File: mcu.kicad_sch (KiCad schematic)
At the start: 14 parts, among them U4 STM32F070RBTx, Y2 XRCGB32M000F2P01R0

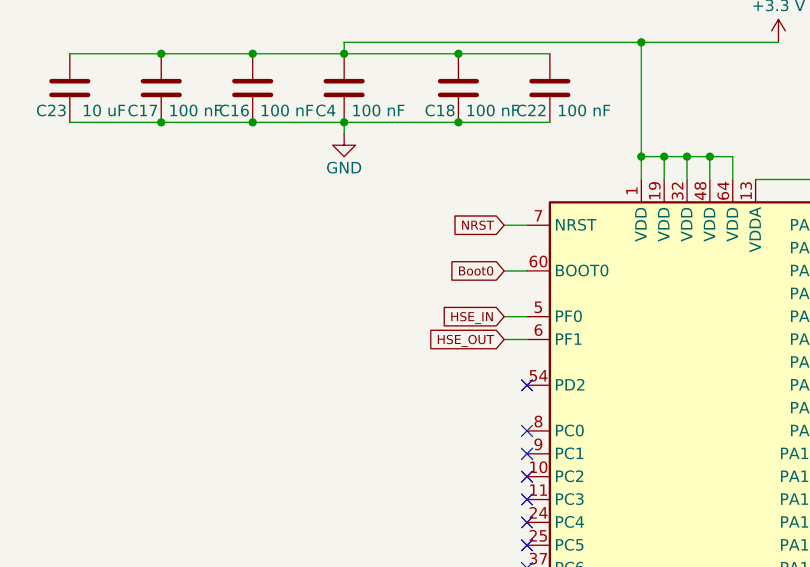
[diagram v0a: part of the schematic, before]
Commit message: removed manual switch
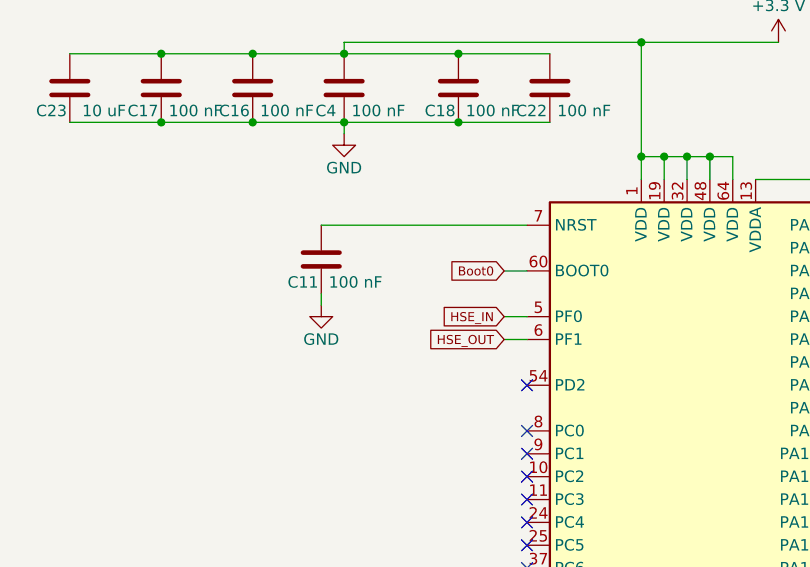
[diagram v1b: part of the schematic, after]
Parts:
- added C11: 100 nF, Capacitor_SMD:C_0805_2012Metric, symbol Device:C
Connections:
- net GND: now also C11.1
- net NRST: no longer names the net of U4.7 (NRST)
- net NRST: now also C11.2
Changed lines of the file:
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@@
+	(wire
+		(pts
+			(xy 63.5 66.04) (xy 63.5 67.31)
+		)
+		(stroke
+			(width 0)
+			(type default)
+		)
+	)
 	(wire
 		(pts
@@
 	(wire
 		(pts
+			(xy 63.5 58.42) (xy 86.36 58.42)
+		)
+		(stroke
+			(width 0)
+			(type default)
+		)
+	)
+	(wire
+		(pts
 			(xy 204.47 91.44) (xy 204.47 86.36)
 		)
@@
 		(pts
 			(xy 101.6 53.34) (xy 101.6 50.8)
-		)
-		(stroke
-			(width 0)
-			(type default)
-		)
-	)
-	(wire
-		(pts
-			(xy 83.82 58.42) (xy 86.36 58.42)
 		)
 		(stroke
@@
 		)
 	)
-	(global_label "NRST"
-		(shape input)
-		(at 83.82 58.42 180)
-		(fields_autoplaced yes)
-		(effects
-			(font
-				(size 1 1)
-			)
-			(justify right)
-		)
-		(property "Intersheetrefs" "${INTERSHEET_REFS}"
-			(at 77.7078 58.42 0)
-			(effects
-				(font
-					(size 1.27 1.27)
-				)
-				(justify right)
-				(hide yes)
-			)
-		)
-	)
 	(global_label "USART1_RX"
 		(shape input)
@@
 	(symbol
 		(lib_id "power:GND")
+		(at 63.5 67.31 0)
+		(unit 1)
+		(exclude_from_sim no)
+		(in_bom yes)
+		(on_board yes)
+		(dnp no)
+		(property "Reference" "#PWR021"
+			(at 63.5 73.66 0)
+			(effects
+				(font
+					(size 1.27 1.27)
+				)
+				(hide yes)
+			)
+		)
+		(property "Value" "GND"
+			(at 63.5 71.12 0)
+			(effects
+				(font
+					(size 1.27 1.27)
+				)
+			)
+		)
+		(property "Footprint" ""
+			(at 63.5 67.31 0)
+			(effects
+				(font
+					(size 1.27 1.27)
+				)
+				(hide yes)
+			)
+		)
+		(property "Datasheet" ""
+			(at 63.5 67.31 0)
+			(effects
+				(font
+					(size 1.27 1.27)
+				)
+				(hide yes)
+			)
+		)
+		(property "Description" "Power symbol creates a global label with name \"GND\" , ground"
+			(at 63.5 67.31 0)
+			(effects
+				(font
+					(size 1.27 1.27)
+				)
+				(hide yes)
+			)
+		)
+		(pin "1"
+		)
+		(instances
+			(project "apex"
+				(path "/84b8b555-aaa5-476b-b0f2-2d0f894bf0e6/365404b6-d1fa-4571-8ebc-5e079dd57407"
+					(reference "#PWR021")
+					(unit 1)
+				)
+			)
+		)
+	)
+	(symbol
+		(lib_id "power:GND")
 		(at 137.16 63.5 0)
 		(unit 1)
@@
 					(unit 1)
 				)
+			)
+		)
+	)
+	(symbol
+		(lib_id "Device:C")
+		(at 63.5 62.23 180)
+		(unit 1)
+		(exclude_from_sim no)
+		(in_bom yes)
+		(on_board yes)
+		(dnp no)
+		(property "Reference" "C11"
+			(at 61.468 64.77 0)
+			(effects
+				(font
+					(size 1.27 1.27)
+				)
+			)
+		)
+		(property "Value" "100 nF"
+			(at 67.31 64.77 0)
+			(effects
+				(font
+					(size 1.27 1.27)
+				)
+			)
+		)
+		(property "Footprint" "Capacitor_SMD:C_0805_2012Metric"
+			(at 62.5348 58.42 0)
+			(effects
+				(font
+					(size 1.27 1.27)
+				)
+				(hide yes)
+			)
+		)
+		(property "Datasheet" "~"
+			(at 63.5 62.23 0)
+			(effects
+				(font
+					(size 1.27 1.27)
+				)
+				(hide yes)
+			)
+		)
+		(property "Description" "Unpolarized capacitor"
+			(at 63.5 62.23 0)
+			(effects
+				(font
+					(size 1.27 1.27)
+				)
+				(hide yes)
+			)
+		)
+		(pin "1"
+		)
+		(pin "2"
+		)
+		(instances
+			(project "apex"
+				(path "/84b8b555-aaa5-476b-b0f2-2d0f894bf0e6/365404b6-d1fa-4571-8ebc-5e079dd57407"
+					(reference "C11")
+					(unit 1)
+				)

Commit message: removed AVR mcu
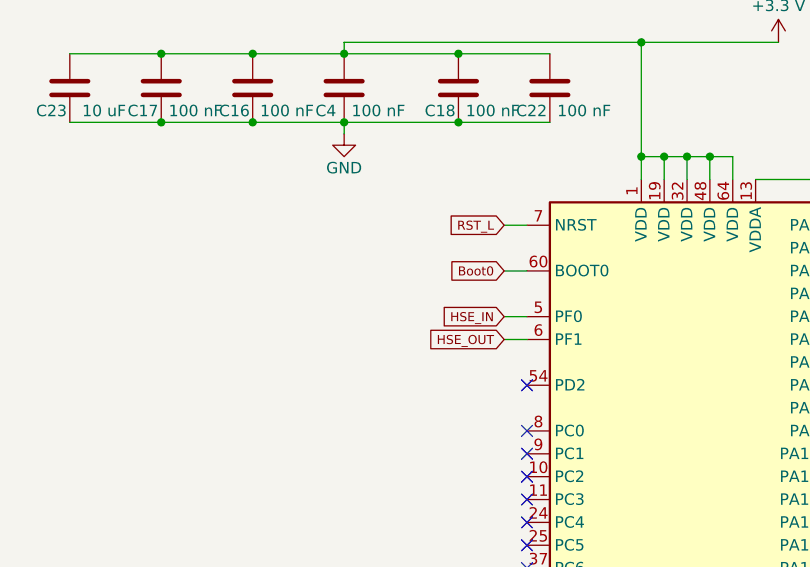
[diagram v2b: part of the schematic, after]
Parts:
- removed C11: 100 nF, Capacitor_SMD:C_0805_2012Metric, symbol Device:C
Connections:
- net RST_L: now reaches U4.7 (NRST)
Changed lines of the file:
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@@
-	(wire
-		(pts
-			(xy 63.5 66.04) (xy 63.5 67.31)
-		)
-		(stroke
-			(width 0)
-			(type default)
-		)
-	)
 	(wire
 		(pts
@@
 	(wire
 		(pts
-			(xy 63.5 58.42) (xy 86.36 58.42)
-		)
-		(stroke
-			(width 0)
-			(type default)
-		)
-	)
-	(wire
-		(pts
 			(xy 204.47 91.44) (xy 204.47 86.36)
 		)
@@
 		(pts
 			(xy 121.92 83.82) (xy 124.46 83.82)
+		)
+		(stroke
+			(width 0)
+			(type default)
+		)
+	)
+	(wire
+		(pts
+			(xy 83.82 58.42) (xy 86.36 58.42)
 		)
 		(stroke
@@
 				)
 				(justify left)
+				(hide yes)
+			)
+		)
+	)
+	(global_label "RST_L"
+		(shape input)
+		(at 83.82 58.42 180)
+		(fields_autoplaced yes)
+		(effects
+			(font
+				(size 1 1)
+			)
+			(justify right)
+		)
+		(property "Intersheetrefs" "${INTERSHEET_REFS}"
+			(at 77.184 58.42 0)
+			(effects
+				(font
+					(size 1.27 1.27)
+				)
+				(justify right)
 				(hide yes)
 			)
@@
 				(path "/84b8b555-aaa5-476b-b0f2-2d0f894bf0e6/365404b6-d1fa-4571-8ebc-5e079dd57407"
 					(reference "#PWR038")
-					(unit 1)
-				)
-			)
-		)
-	)
-	(symbol
-		(lib_id "power:GND")
-		(at 63.5 67.31 0)
-		(unit 1)
-		(exclude_from_sim no)
-		(in_bom yes)
-		(on_board yes)
-		(dnp no)
-		(property "Reference" "#PWR021"
-			(at 63.5 73.66 0)
-			(effects
-				(font
-					(size 1.27 1.27)
-				)
-				(hide yes)
-			)
-		)
-		(property "Value" "GND"
-			(at 63.5 71.12 0)
-			(effects
-				(font
-					(size 1.27 1.27)
-				)
-			)
-		)
-		(property "Footprint" ""
-			(at 63.5 67.31 0)
-			(effects
-				(font
-					(size 1.27 1.27)
-				)
-				(hide yes)
-			)
-		)
-		(property "Datasheet" ""
-			(at 63.5 67.31 0)
-			(effects
-				(font
-					(size 1.27 1.27)
-				)
-				(hide yes)
-			)
-		)
-		(property "Description" "Power symbol creates a global label with name \"GND\" , ground"
-			(at 63.5 67.31 0)
-			(effects
-				(font
-					(size 1.27 1.27)
-				)
-				(hide yes)
-			)
-		)
-		(pin "1"
-		)
-		(instances
-			(project "apex"
-				(path "/84b8b555-aaa5-476b-b0f2-2d0f894bf0e6/365404b6-d1fa-4571-8ebc-5e079dd57407"
-					(reference "#PWR021")
 					(unit 1)
 				)
@@
 					(unit 1)
 				)
-			)
-		)
-	)
-	(symbol
-		(lib_id "Device:C")
-		(at 63.5 62.23 180)
-		(unit 1)
-		(exclude_from_sim no)
-		(in_bom yes)
-		(on_board yes)
-		(dnp no)
-		(property "Reference" "C11"
-			(at 61.468 64.77 0)
-			(effects
-				(font
-					(size 1.27 1.27)
-				)
-			)
-		)
-		(property "Value" "100 nF"
-			(at 67.31 64.77 0)
-			(effects
-				(font
-					(size 1.27 1.27)
-				)
-			)
-		)
-		(property "Footprint" "Capacitor_SMD:C_0805_2012Metric"
-			(at 62.5348 58.42 0)
-			(effects
-				(font
-					(size 1.27 1.27)
-				)
-				(hide yes)
-			)
-		)
-		(property "Datasheet" "~"
-			(at 63.5 62.23 0)
-			(effects
-				(font
-					(size 1.27 1.27)
-				)
-				(hide yes)
-			)
-		)
-		(property "Description" "Unpolarized capacitor"
-			(at 63.5 62.23 0)
-			(effects
-				(font
-					(size 1.27 1.27)
-				)
-				(hide yes)
-			)
-		)
-		(pin "1"
-		)
-		(pin "2"
-		)
-		(instances
-			(project "apex"
-				(path "/84b8b555-aaa5-476b-b0f2-2d0f894bf0e6/365404b6-d1fa-4571-8ebc-5e079dd57407"
-					(reference "C11")
-					(unit 1)
-				)

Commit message: added diode
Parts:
- removed C5, C6: 8 pF, Capacitor_SMD:C_0805_2012Metric, symbol Device:C
- removed Y2: XRCGB32M000F2P01R0, XRCGB32M000F2P01R0:OSC_XRCGB32M000F2P01R0, symbol XRCGB32M000F2P01R0:XRCGB32M000F2P01R0
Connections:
- net +3.3 V renamed VMCU
- net +3.3 VA renamed +3.3VA
- net HSE_IN renamed CLK_32MHZ
- net HSE_OUT: no longer names the net of U4.6 (PF1)
- no-connect marks 41 -> 42
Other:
- note removed: "High-Speed Oscillator"

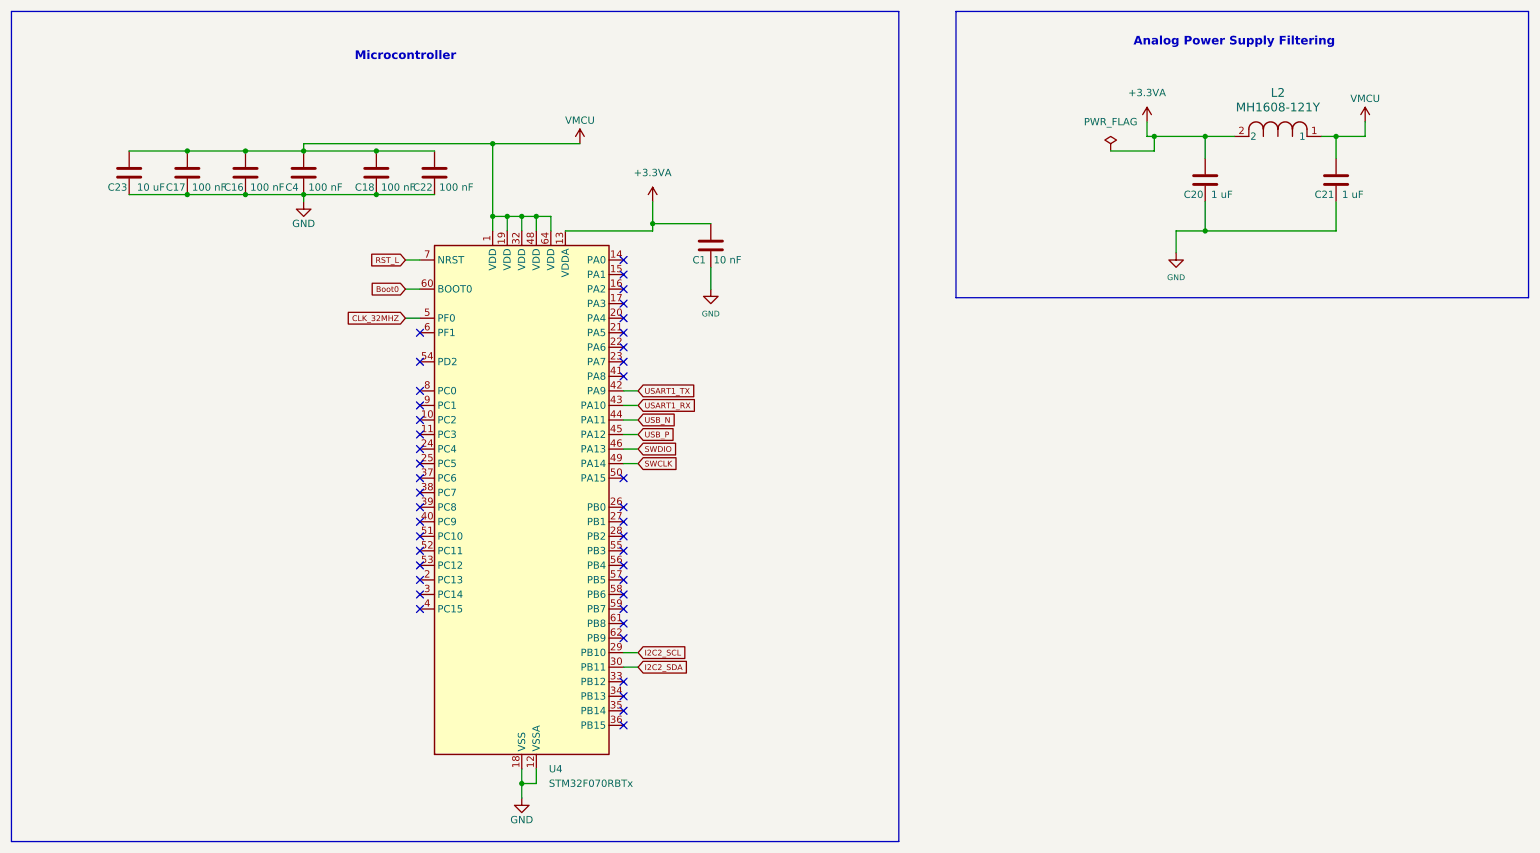
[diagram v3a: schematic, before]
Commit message: separated voltage source labels
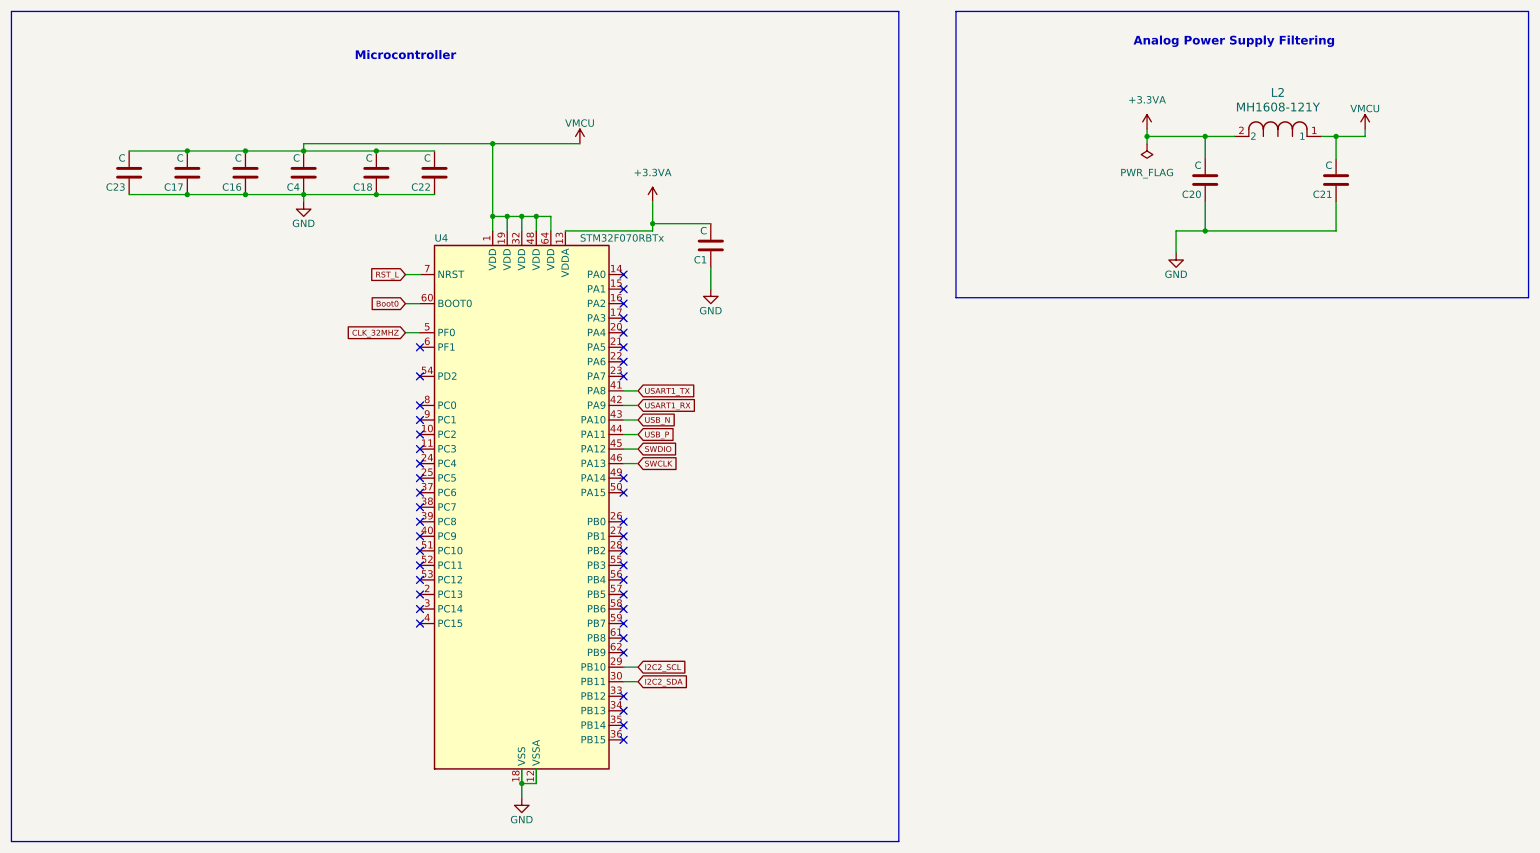
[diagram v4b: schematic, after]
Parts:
- C1: value 10 nF -> C
- C16, C17, C18, C22, C4: value 100 nF -> C
- C20, C21: value 1 uF -> C
- C23: value 10 uF -> C
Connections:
- net SWCLK: now also U4.46 (PA13); no longer U4.49 (PA14)
- net SWDIO: now also U4.45 (PA12); no longer U4.46 (PA13)
- net USART1_RX: now also U4.42 (PA9); no longer U4.43 (PA10)
- net USART1_TX: now also U4.41 (PA8); no longer U4.42 (PA9)
- net USB_N: now also U4.43 (PA10); no longer U4.44 (PA11)
- net USB_P: now also U4.44 (PA11); no longer U4.45 (PA12)
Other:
- moved on the sheet: U4

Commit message: isolated v sources
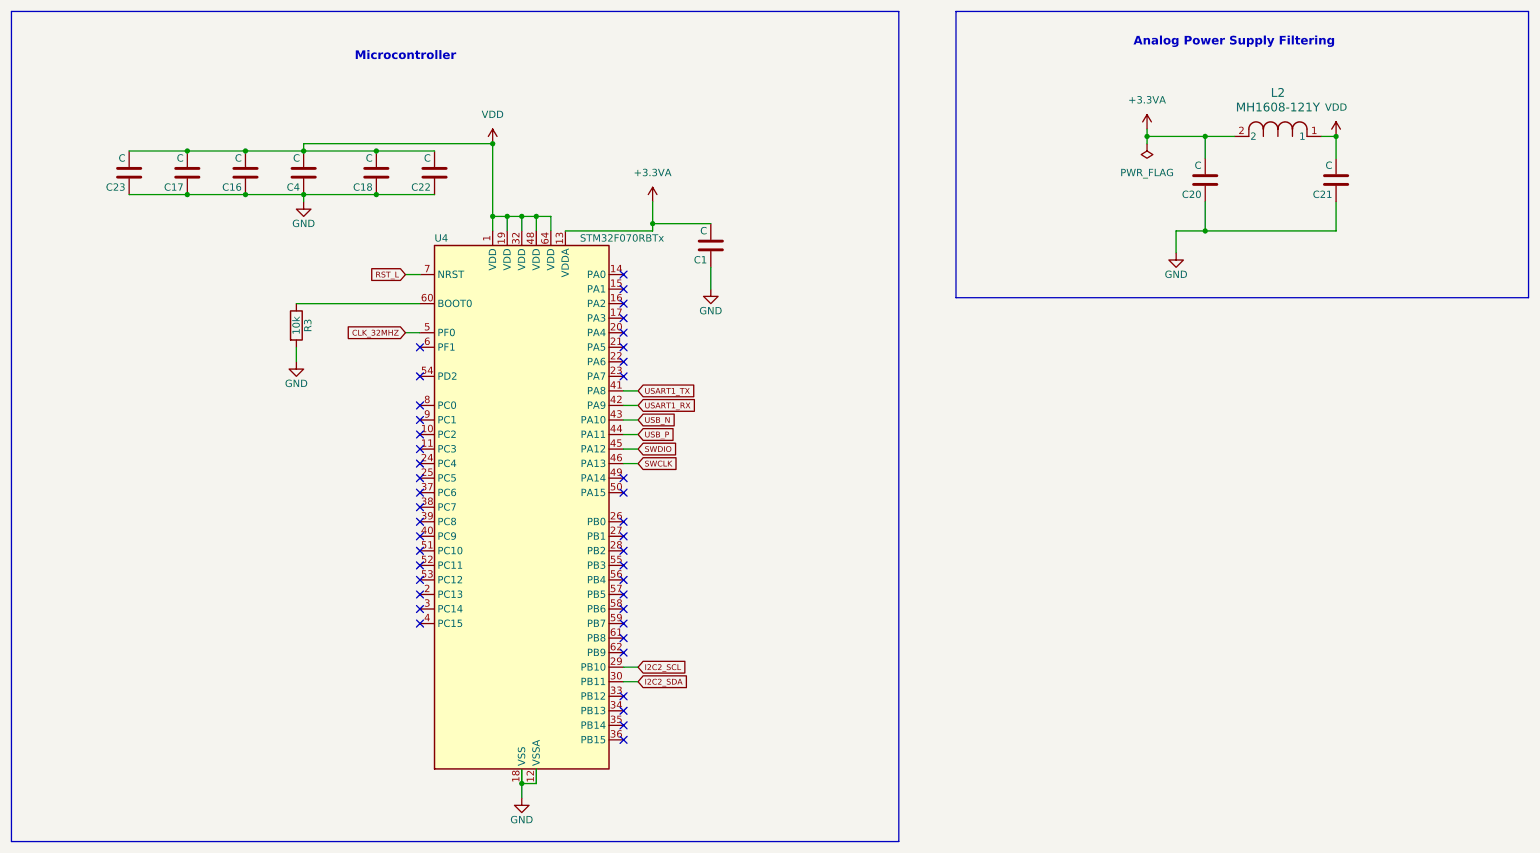
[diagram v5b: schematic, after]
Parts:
- added R3: 10k, Resistor_SMD:R_0805_2012Metric, symbol Device:R
- L2: footprint MH1608:IND_BOURNS_MH1608 -> IND_BOURNS_MH1608; symbol MH1608_121Y:MH1608-121Y -> FER_F0603F120:MH1608-121Y
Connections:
- net GND: now also R3.2
- net Boot0: no longer names the net of U4.60 (BOOT0)
- net Boot0: now also R3.1
- net VMCU renamed VDD

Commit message: added sheets
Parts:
- L2: footprint IND_BOURNS_MH1608 -> FERR_0603_120:IND_BOURNS_MH1608
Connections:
- net Boot0: now reaches R3.1, U4.60 (BOOT0)
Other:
- moved on the sheet: C20, C21, L2
